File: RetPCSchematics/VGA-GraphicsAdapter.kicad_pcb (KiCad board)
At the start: 2 copper layers, 136.7 x 101.3 mm, 41 parts, among them J1 Bus_ISA_8bit, J2 74320-9004, J3 Conn_01x02_Male, U1 74AUC2G125, U10 ATmega644P-20PU, U11 628128, U12 628128, U13 SN74LVC245AN, U14 74LS245, U15 74LVC2G240, U16 74LVC2G240, U17 74LVC1G18, U18 74LVC1G18, U19 74LVC1G18, U2 74LVC2G240, U20 74LVC1G18, U21 ATF22V10D, U22 74LS245, U23 74LVC1G373, U24 74LVC1G373, U25 74LVC1G373, U26 74LVC1G373, U27 74LVC1G373, U28 74LVC1G373, U29 74LVC1G373, U3 ATF22V10D, U30 74LVC1G373, U31 74LVC1G373, U32 74LVC1G373, U33 74LVC1G373, U34 74LVC1G373, U36 TFP410, U37 ATF750C, U4 ATF22V10D, U5 74LS245, U6 ATF22V10D, U7 74LS245, U8 74LS245, U9 74LS245, X1 DGOF5S3

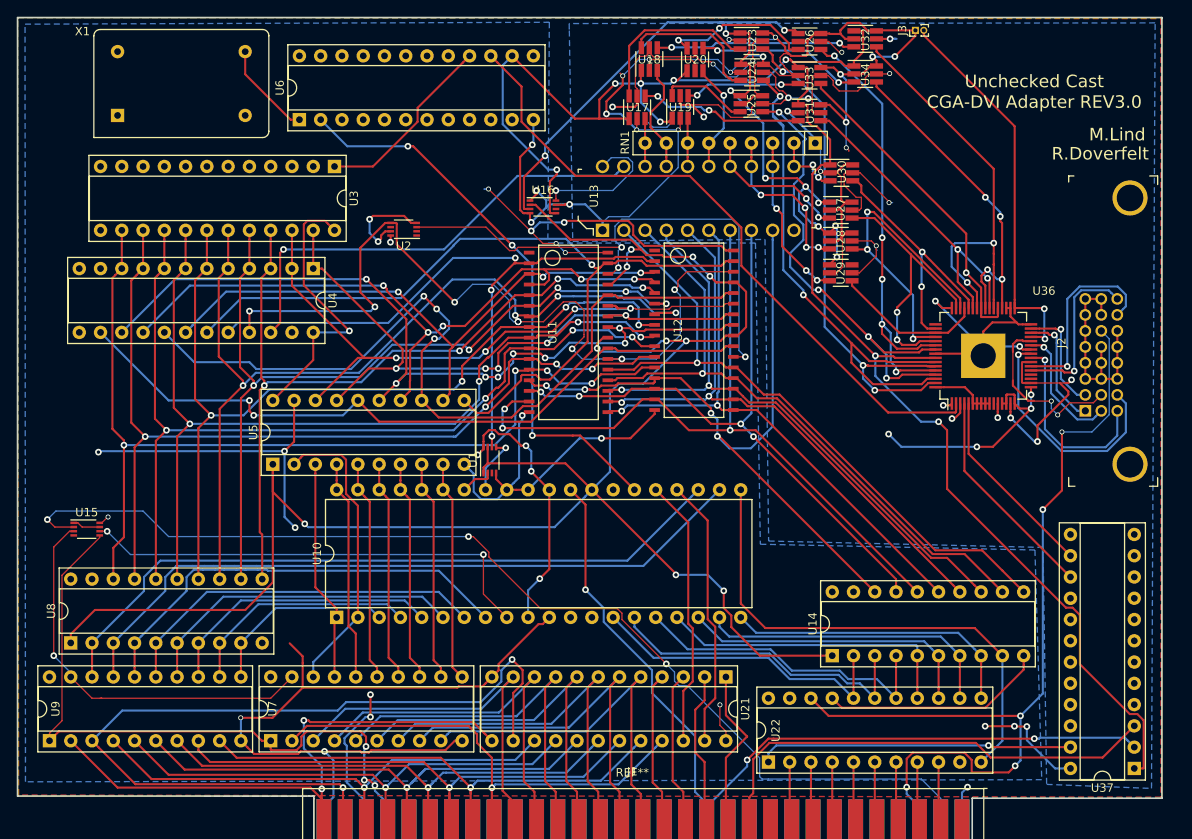
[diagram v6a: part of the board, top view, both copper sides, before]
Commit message: Started on Rev 4.0
started on a +3.3V main circuit. Bigger RAM, can now additionally support EGA and TGA through firmware if memory map doesn't collide in a non compatible way.
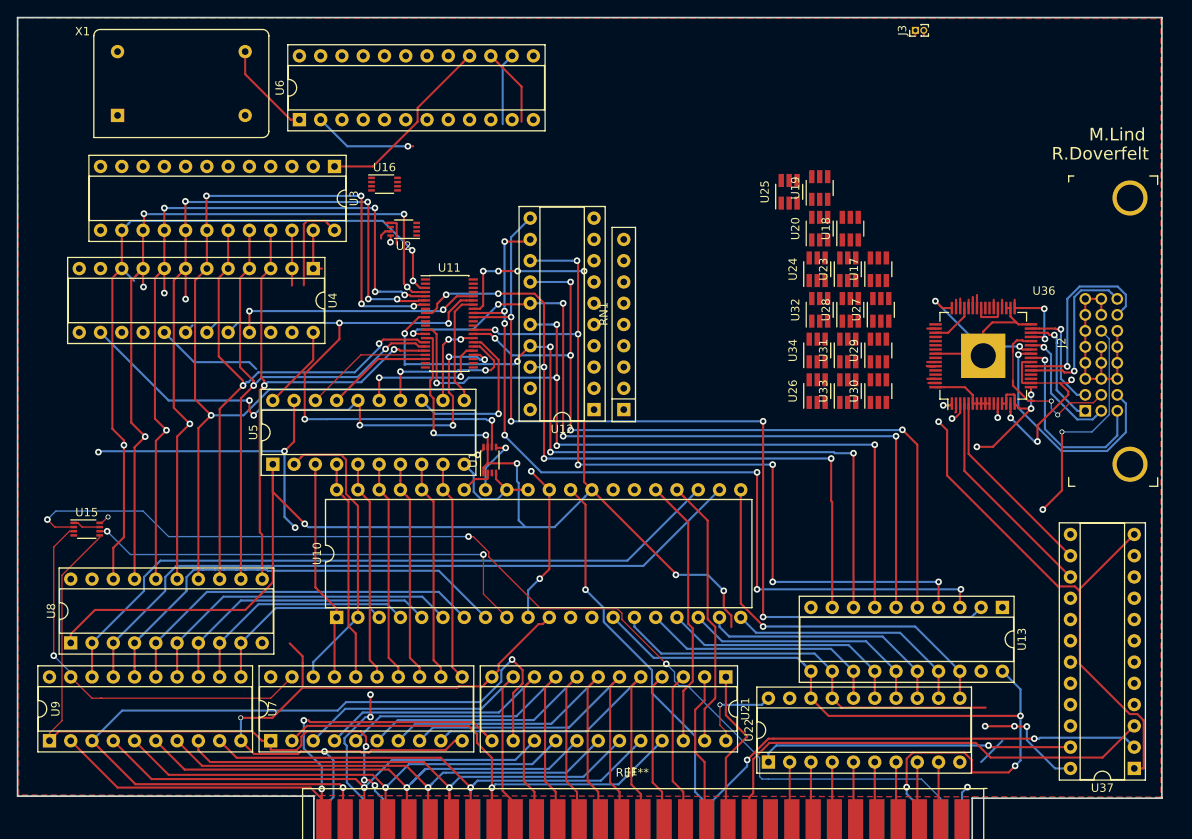
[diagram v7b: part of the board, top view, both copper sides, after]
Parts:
- removed U14: 74LS245, Package_DIP:DIP-20_W7.62mm_Socket
- U11: value 628128 -> IS61LV5128AL-10TLI; footprint SMD_Packages:SOJ-32 -> Package_SO:TSSOP-44_4.4x11.2mm_P0.5mm
- U12: value 628128 -> 74LS245; footprint SMD_Packages:SOJ-32 -> Package_DIP:DIP-20_W7.62mm_Socket
- U13: footprint digikey-footprints:DIP-20_W7.62mm -> Package_DIP:DIP-20_W7.62mm_Socket
- U22: value 74LS245 -> 74LS245A; footprint Package_DIP:DIP-22_W7.62mm_Socket -> Package_DIP:DIP-20_W7.62mm_Socket
- U7, U9: value 74LS245 -> 74LS245A
- moved U13 65.6 mm to (228.6, 116.2), turned to 270 degrees
- moved U26 41.8 mm to (206.5, 90.3), turned to 90 degrees
- moved RN1 39.2 mm to (183.4, 92.5), turned to 90 degrees
- moved U33 38.0 mm to (210.1, 90.3), turned to 90 degrees
- moved U17 34.7 mm to (213.8, 75.8)
- moved U34 33.5 mm to (206.5, 85.5), turned to 90 degrees
- moved U32 32.8 mm to (206.8, 80.6), turned to 90 degrees
- moved U18 31.4 mm to (210.4, 70.9)
- moved U23 29.6 mm to (210.1, 75.8), turned to 90 degrees
- moved U31 28.8 mm to (210.1, 85.5), turned to 90 degrees
- moved U30 26.4 mm to (213.8, 90.3), turned to 90 degrees
- moved U20 25.1 mm to (206.8, 70.9)
- moved U24 24.8 mm to (206.5, 75.8), turned to 90 degrees
- moved U19 19.3 mm to (206.8, 66.1)
- moved U16 19.1 mm to (154.8, 65.6)
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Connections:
- J1 pad 1: GND -> GClock
- J1 pad 29: +5V -> +3V3
- J1 pad 3: +5V -> +3V3
- J1 pad 31: GND -> GClock
- J2 pad 11: GND -> GClock
- J2 pad 12: GND -> GClock
- J2 pad 13: GND -> GClock
- J2 pad 14: +5V -> +3V3
- J2 pad 15: GND -> GClock
- J2 pad 16: GND -> GClock
- J2 pad 19: GND -> GClock
- J2 pad 20: GND -> GClock
- J2 pad 21: GND -> GClock
- J2 pad 22: GND -> GClock
- J2 pad 3: GND -> GClock
- J2 pad 4: GND -> GClock
- J2 pad 5: GND -> GClock
- J2 pad 6: GND -> GClock
- J2 pad 7: GND -> GClock
- J2 pad 8: GND -> GClock
- J3 pad 1: GND -> GClock
- RN1 pad 1: GND -> GClock
- U1 pad 4: GND -> GClock
- U1 pad 8: +5V -> +3V3
- U10 pad 10: +5V -> +3V3
- U10 pad 11: GND -> GClock
- U10 pad 24: Sel -> /XA18
- U10 pad 25: REG -> Sel
- U10 pad 26: OP -> REG
- U10 pad 27: CountReset -> OP
- U10 pad 30: +5V -> +3V3
- U10 pad 31: GND -> GClock
- U10 pad 32: GND -> GClock
- U11 pad 1: (no net) -> Net-(U11-Pad1)
- U11 pad 10: /VA2 -> /D1
- U11 pad 11: /VA1 -> +3V3
- U11 pad 12: /VA0 -> GClock
- U11 pad 13: /D0 -> /D2
- U11 pad 14: /D1 -> /D3
- U11 pad 15: /D2 -> LoadEnable
- U11 pad 16: GND -> /VA5
- U11 pad 17: /D3 -> /VA6
- U11 pad 18: /D4 -> /VA7
- U11 pad 19: /D5 -> /VA8
- U11 pad 2: /VA16 -> Net-(U11-Pad2)
- U11 pad 20: /D6 -> /VA9
- U11 pad 21: /D7 -> Net-(U11-Pad21)
- U11 pad 22: CS -> Net-(U11-Pad22)
- U11 pad 23: /VA10 -> Net-(U11-Pad23)
- U11 pad 24: LoadEnable -> Net-(U11-Pad24)
- U11 pad 25: /VA11 -> Net-(U11-Pad25)
- U11 pad 26: /VA9 -> /VA10
- U11 pad 27: /VA8 -> /VA11
- U11 pad 28: /VA13 -> /VA12
- U11 pad 29: LoadEnable -> /VA13
- U11 pad 3: /VA14 -> /VA0
- U11 pad 30: CS(inv) -> /VA14
- U11 pad 31: /VA15 -> /D4
- U11 pad 32: +5V -> /D5
- U11 pad 4: /VA12 -> /VA1
- U11 pad 5: /VA7 -> /VA2
- U11 pad 6: /VA6 -> /VA3
- U11 pad 7: /VA5 -> /VA4
- U11 pad 8: /VA4 -> GClock
- U11 pad 9: /VA3 -> /D0
- U12 pad 1: (no net) -> GClock
- U12 pad 10: /VA2 -> GClock
- U12 pad 11: /VA1 -> /D7
- U12 pad 12: /VA0 -> /D6
- U12 pad 13: /D0 -> /D5
- U12 pad 14: /D1 -> /D4
- U12 pad 15: /D2 -> /D3
- U12 pad 16: GND -> /D2
- U12 pad 17: /D3 -> /D1
- U12 pad 18: /D4 -> /D0
- U12 pad 19: /D5 -> GEnd(inv)
- U12 pad 2: /VA16 -> Net-(RN1-Pad2)
- U12 pad 20: /D6 -> +3V3
- U12 pad 3: /VA14 -> Net-(RN1-Pad3)
- U12 pad 4: /VA12 -> Net-(RN1-Pad4)
- U12 pad 5: /VA7 -> Net-(RN1-Pad5)
- U12 pad 6: /VA6 -> Net-(RN1-Pad6)
- U12 pad 7: /VA5 -> Net-(RN1-Pad7)
- U12 pad 8: /VA4 -> Net-(RN1-Pad8)
- U12 pad 9: /VA3 -> Net-(RN1-Pad9)
- U13 pad 1: GND -> Net-(U13-Pad1)
- U13 pad 10: GND -> GClock
- U13 pad 11: Net-(RN1-Pad2) -> Net-(U10-Pad14)
- U13 pad 12: Net-(RN1-Pad3) -> Net-(U10-Pad15)
- U13 pad 13: Net-(RN1-Pad4) -> Net-(U10-Pad16)
- U13 pad 14: Net-(RN1-Pad5) -> Net-(U10-Pad17)
- U13 pad 15: Net-(RN1-Pad6) -> Net-(U10-Pad18)
- U13 pad 16: Net-(RN1-Pad7) -> Net-(U10-Pad19)
- U13 pad 17: Net-(RN1-Pad8) -> Net-(U10-Pad20)
- U13 pad 18: Net-(RN1-Pad9) -> Net-(U10-Pad21)
- U13 pad 19: GEnd -> Net-(U13-Pad19)
- U15 pad 1: GND -> GClock
- U15 pad 4: GND -> GClock
- U15 pad 7: GND -> GClock
- U15 pad 8: +5V -> +3V3
- U16 pad 1: GND -> GClock
- U16 pad 4: GND -> GClock
- U16 pad 7: GND -> GClock
- U17 pad 2: GND -> GClock
- U18 pad 2: GND -> GClock
- U19 pad 2: GND -> GClock
- U2 pad 1: (no net) -> GClock
- U2 pad 2: (no net) -> /XA18
- U2 pad 3: CS(inv) -> GEnd(inv)
- U2 pad 4: GND -> GClock
- U2 pad 5: CS -> GEnd
- U2 pad 6: (no net) -> /VA18
- U2 pad 7: GND -> GClock
- U2 pad 8: +5V -> +3V3
- U20 pad 2: GND -> GClock
- U21 pad 12: GND -> GClock
- U21 pad 24: +5V -> +3V3
- U22 pad 10: GND -> GClock
- U22 pad 19: GND -> GClock
- U22 pad 20: +5V -> +3V3
- U23 pad 2: GND -> GClock
- U23 pad 6: GND -> GClock
- U24 pad 2: GND -> GClock
- U24 pad 6: GND -> GClock
- U25 pad 2: GND -> GClock
- U25 pad 6: GND -> GClock
- U26 pad 2: GND -> GClock
- U26 pad 6: GND -> GClock
- U27 pad 2: GND -> GClock
- U27 pad 6: GND -> GClock
- U28 pad 2: GND -> GClock
- U28 pad 6: GND -> GClock
- U29 pad 2: GND -> GClock
- U3 pad 12: GND -> GClock
- U3 pad 24: +5V -> +3V3
- U30 pad 2: GND -> GClock
- U30 pad 6: GND -> GClock
- U31 pad 2: GND -> GClock
- U31 pad 6: GND -> GClock
- U32 pad 2: GND -> GClock
- U32 pad 6: GND -> GClock
- U33 pad 2: GND -> GClock
- U33 pad 6: GND -> GClock
- U34 pad 2: GND -> GClock
- U34 pad 6: GND -> GClock
- U36 pad 10: GND -> GClock
- U36 pad 13: GND -> GClock
- U36 pad 14: GND -> GClock
- U36 pad 16: GND -> GClock
- U36 pad 17: GND -> GClock
- U36 pad 20: GND -> GClock
- U36 pad 26: GND -> GClock
- U36 pad 32: GND -> GClock
- U36 pad 34: GND -> GClock
- U36 pad 35: GND -> GClock
- U36 pad 48: GND -> GClock
- U36 pad 56: GND -> GClock
- U36 pad 57: GClock -> Net-(U36-Pad57)
- U36 pad 6: GND -> GClock
- U36 pad 64: GND -> GClock
- U36 pad 65: GND -> GClock
- U36 pad 7: GND -> GClock
- U36 pad 8: GND -> GClock
- U36 pad 9: GND -> GClock
- U37 pad 12: GND -> GClock
- U4 pad 12: GND -> GClock
- U4 pad 21: CS -> /VA17
- U4 pad 22: GEnd -> /VA18
- U4 pad 23: Net-(U4-Pad23) -> GEnd
- U4 pad 24: +5V -> +3V3
- U5 pad 10: GND -> GClock
- U5 pad 19: GND -> GClock
- U5 pad 20: +5V -> +3V3
- U6 pad 12: GND -> GClock
- U6 pad 24: +5V -> +3V3
- U7 pad 10: GND -> GClock
- U7 pad 20: +5V -> +3V3
- U8 pad 10: GND -> GClock
- U8 pad 19: GND -> GClock
- U8 pad 20: +5V -> +3V3
- U9 pad 10: GND -> GClock
- U9 pad 20: +5V -> +3V3
- X1 pad 14: +5V -> +3V3
- X1 pad 7: GND -> GClock
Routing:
- net GND: track 527.8 -> 0.00 mm, vias 36 -> 0
- net +5V: track 245.3 -> 0.00 mm, vias 20 -> 0
- net GClock: track 210.3 -> 311.7 mm, vias 8 -> 12
- net CS: track 99.6 -> 0.00 mm, vias 8 -> 0
- net Net-(U16-Pad3): track 97.1 -> 0.00 mm, vias 10 -> 0
- net /VA15: track 99.5 -> 15.2 mm, vias 1 -> 0
- net /VA11: track 98.3 -> 16.7 mm, vias 8 -> 2
- net DE: track 79.4 -> 10.5 mm
- net /VA13: track 99.3 -> 33.0 mm, vias 3 -> 1
- net CS(inv): track 65.8 -> 0.00 mm, vias 3 -> 0
- net /VA12: track 83.3 -> 18.8 mm, vias 5 -> 2
- net Net-(U24-Pad4): track 65.5 -> 2.00 mm, vias 2 -> 0
- net Net-(U23-Pad4): track 64.3 -> 2.80 mm, vias 3 -> 0
- net /VA14: track 71.7 -> 11.7 mm, vias 3 -> 2
- net /VA8: track 80.9 -> 22.0 mm, vias 4 -> 0
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- added copper zone on F.Cu, net GClock
- removed copper zone on B.Cu, net +3V3
- removed copper zone on B.Cu, net +5V
- removed copper zone on F.Cu, net GND
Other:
- board text removed: "CGA-DVI Adapter REV3.0"
- board text removed: "Unchecked Cast"

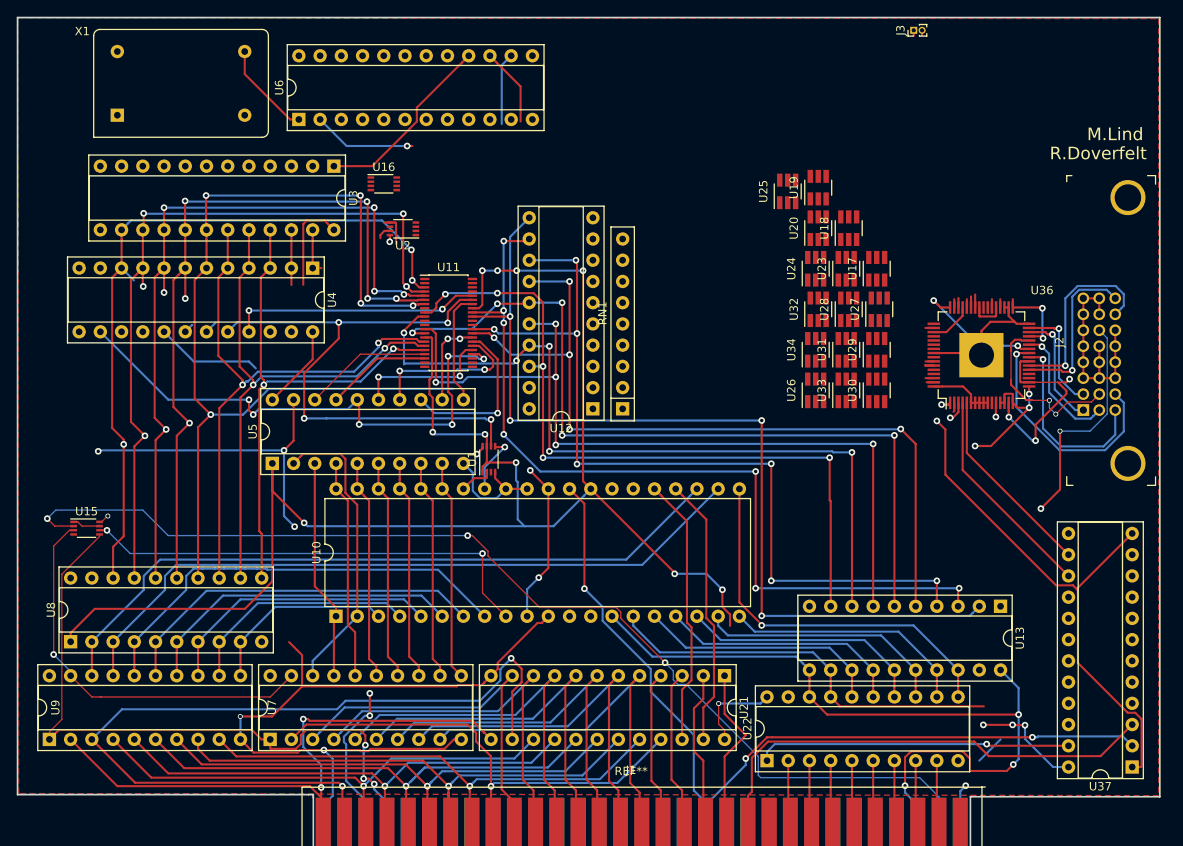
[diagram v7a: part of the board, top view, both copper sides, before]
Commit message: Fixed some schematics errors, EOD sync
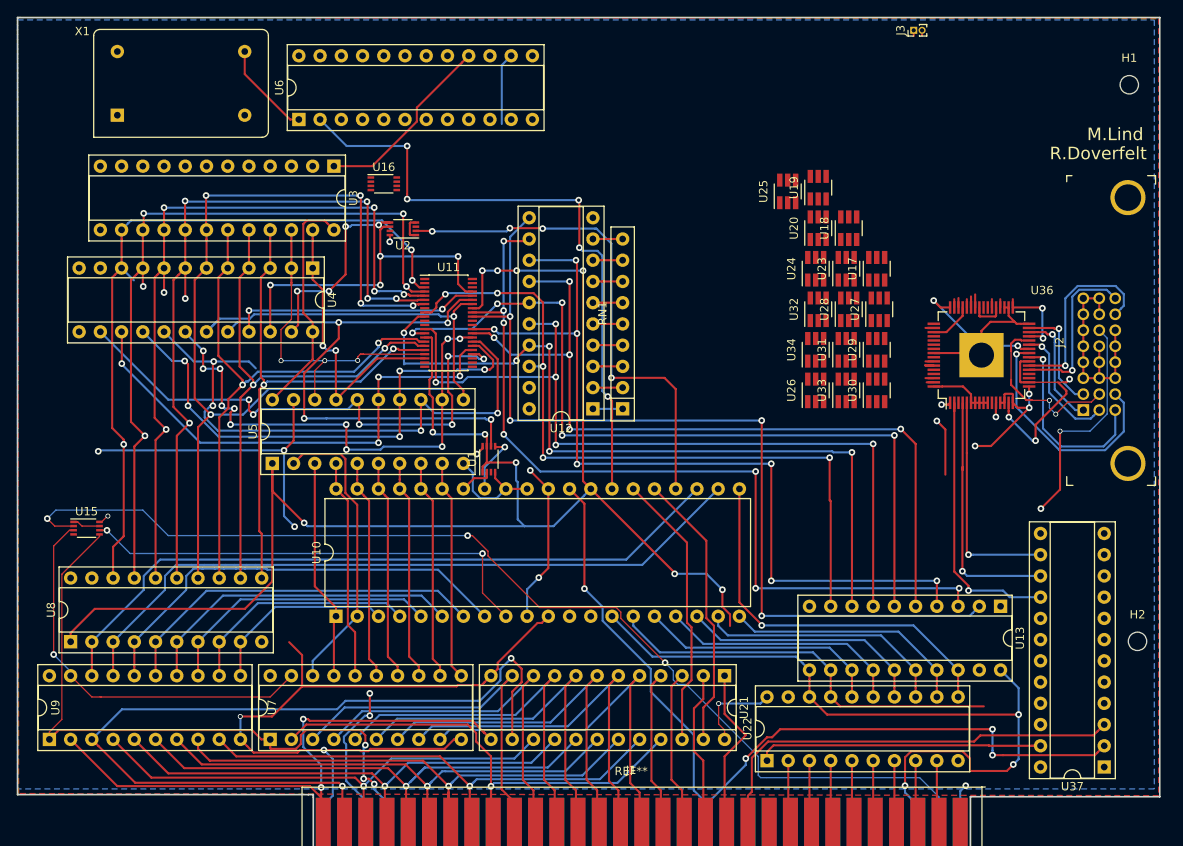
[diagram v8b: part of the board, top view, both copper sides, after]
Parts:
- added H1: MountingHole, MountingHole:MountingHole_2.2mm_M2, F.Cu at (244.0, 53.8)
- added H2: MountingHole, MountingHole:MountingHole_2.2mm_M2, F.Cu at (245.0, 120.3)
- moved U37 3.35 mm to (241.0, 135.4)
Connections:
- J1 pad 1: GClock -> GND
- J1 pad 31: GClock -> GND
- J2 pad 11: GClock -> GND
- J2 pad 12: GClock -> GND
- J2 pad 13: GClock -> GND
- J2 pad 15: GClock -> GND
- J2 pad 16: GClock -> GND
- J2 pad 19: GClock -> GND
- J2 pad 20: GClock -> GND
- J2 pad 21: GClock -> GND
- J2 pad 22: GClock -> GND
- J2 pad 3: GClock -> GND
- J2 pad 4: GClock -> GND
- J2 pad 5: GClock -> GND
- J2 pad 6: GClock -> GND
- J2 pad 7: GClock -> GND
- J2 pad 8: GClock -> GND
- J3 pad 1: GClock -> GND
- RN1 pad 1: GClock -> GND
- U1 pad 4: GClock -> GND
- U10 pad 11: GClock -> GND
- U10 pad 31: GClock -> GND
- U10 pad 32: GClock -> GND
- U11 pad 12: GClock -> GND
- U11 pad 34: GClock -> GND
- U11 pad 8: GClock -> GND
- U12 pad 1: GClock -> GND
- U12 pad 10: GClock -> GND
- U13 pad 10: GClock -> GND
- U15 pad 1: GClock -> GND
- U15 pad 4: GClock -> GND
- U15 pad 7: GClock -> GND
- U16 pad 1: GClock -> GND
- U16 pad 4: GClock -> GND
- U16 pad 7: GClock -> GND
- U17 pad 2: GClock -> GND
- U18 pad 2: GClock -> GND
- U19 pad 2: GClock -> GND
- U2 pad 1: GClock -> GND
- U2 pad 4: GClock -> GND
- U2 pad 7: GClock -> GND
- U20 pad 2: GClock -> GND
- U21 pad 12: GClock -> GND
- U22 pad 10: GClock -> GND
- U22 pad 19: GClock -> GND
- U23 pad 2: GClock -> GND
- U23 pad 6: GClock -> GND
- U24 pad 2: GClock -> GND
- U24 pad 6: GClock -> GND
- U25 pad 2: GClock -> GND
- U25 pad 6: GClock -> GND
- U26 pad 2: GClock -> GND
- U26 pad 6: GClock -> GND
- U27 pad 2: GClock -> GND
- U27 pad 6: GClock -> GND
- U28 pad 2: GClock -> GND
- U28 pad 6: GClock -> GND
- U29 pad 2: GClock -> GND
- U3 pad 12: GClock -> GND
- U30 pad 2: GClock -> GND
- U30 pad 6: GClock -> GND
- U31 pad 2: GClock -> GND
- U31 pad 6: GClock -> GND
- U32 pad 2: GClock -> GND
- U32 pad 6: GClock -> GND
- U33 pad 2: GClock -> GND
- U33 pad 6: GClock -> GND
- U34 pad 2: GClock -> GND
- U34 pad 6: GClock -> GND
- U36 pad 10: GClock -> GND
- U36 pad 13: GClock -> GND
- U36 pad 14: GClock -> GND
- U36 pad 16: GClock -> GND
- U36 pad 17: GClock -> GND
- U36 pad 20: GClock -> GND
- U36 pad 26: GClock -> GND
- U36 pad 32: GClock -> GND
- U36 pad 34: GClock -> GND
- U36 pad 35: GClock -> GND
- U36 pad 48: GClock -> GND
- U36 pad 56: GClock -> GND
- U36 pad 57: Net-(U36-Pad57) -> GClock
- U36 pad 6: GClock -> GND
- U36 pad 64: GClock -> GND
- U36 pad 65: GClock -> GND
- U36 pad 7: GClock -> GND
- U36 pad 8: GClock -> GND
- U36 pad 9: GClock -> GND
- U37 pad 12: GClock -> GND
- U37 pad 16: Net-(U37-Pad16) -> DE
- U4 pad 12: GClock -> GND
- U5 pad 10: GClock -> GND
- U5 pad 19: GClock -> GND
- U6 pad 12: GClock -> GND
- U6 pad 15: DE -> Net-(U6-Pad15)
- U7 pad 10: GClock -> GND
- U8 pad 10: GClock -> GND
- U8 pad 19: GClock -> GND
- U9 pad 10: GClock -> GND
- X1 pad 7: GClock -> GND
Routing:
- net GClock: track 311.7 -> 15.5 mm, vias 12 -> 1
- net GND: track 0.00 -> 243.5 mm, vias 0 -> 11
- net OP: track 12.4 -> 75.9 mm, vias 1 -> 5
- net /XA18: track 0.00 -> 60.1 mm, vias 0 -> 4
- net /VA14: track 11.7 -> 60.3 mm, vias 2 -> 11
- net /VA11: track 16.7 -> 60.3 mm, vias 2 -> 4
- net /VA12: track 18.8 -> 62.1 mm, vias 2 -> 5
- net /VA18: track 0.00 -> 41.4 mm, vias 0 -> 4
- net /VA13: track 33.0 -> 70.5 mm, vias 1 -> 4
- net /VA15: track 15.2 -> 45.8 mm, vias 0 -> 1
- net DE: track 10.5 -> 33.1 mm, vias 0 -> 1
- net GEnd: track 3.87 -> 23.7 mm, vias 0 -> 4
- net /VA8: track 22.0 -> 39.8 mm, vias 0 -> 3
- net /VA9: track 18.3 -> 34.7 mm, vias 0 -> 2
- net +3V3: track 218.0 -> 208.4 mm, vias 24 -> 20
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- added copper zone on B.Cu, net +3V3
